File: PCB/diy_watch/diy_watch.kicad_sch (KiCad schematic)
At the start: 48 parts, among them IC1 W25Q16JVUXIQ, J1 USB_B_Micro, SW1 SW_Push, U1 FTE-2CA-V-T/R, U2 DS3231MZ, U3 RP2040, U7 XC6210B332MR, U8 LTC4071EMS8E_PBF, Y1 12MHz_crystal

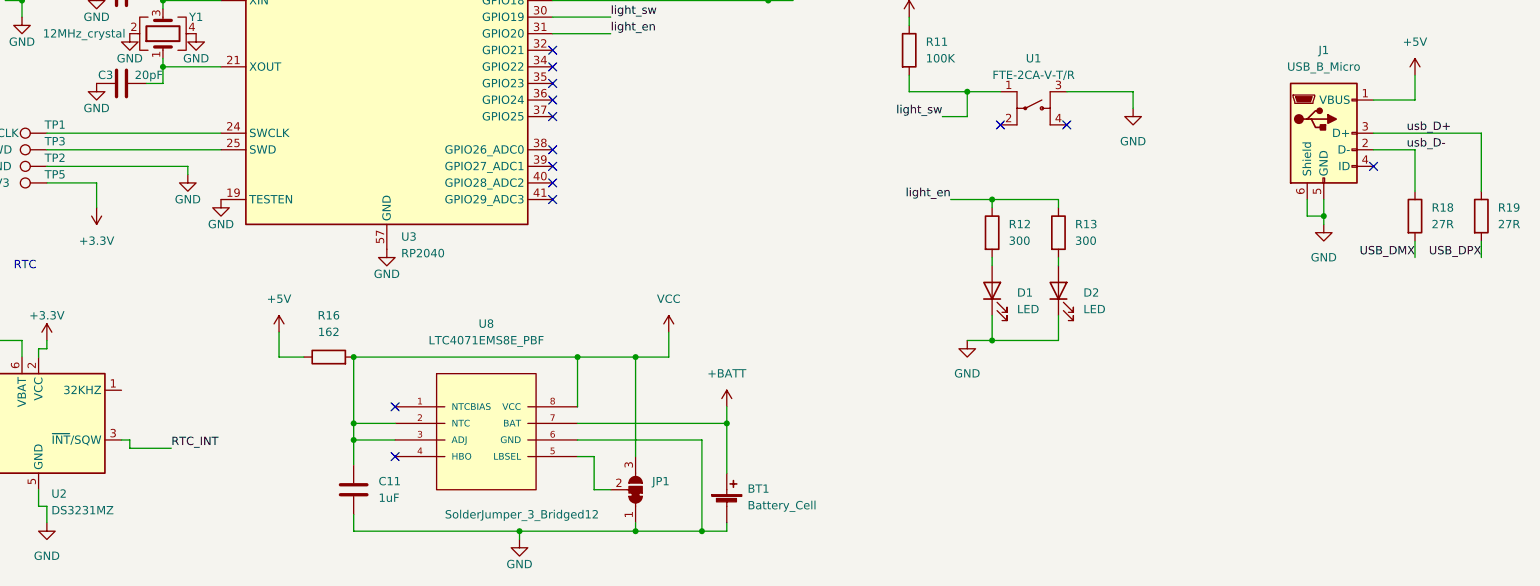
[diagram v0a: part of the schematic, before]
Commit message: Fixing DRC warnings
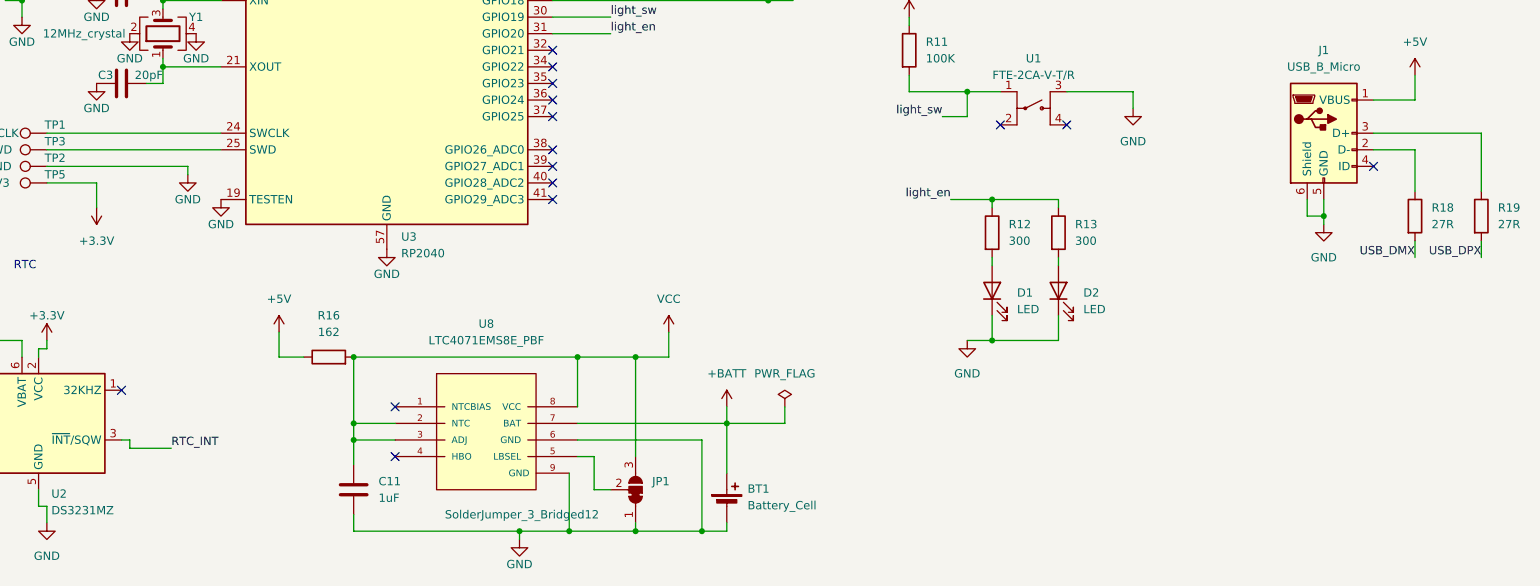
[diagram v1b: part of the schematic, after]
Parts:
- IC1: footprint DIY_Watch_lib:SON50P300X200X60-9N -> W25Q16JVUXIQ:SON50P300X200X60-9N
- U8: footprint Package_SO:MSOP-8-1EP_3x3mm_P0.65mm_EP1.5x1.8mm -> Package_SO:MSOP-8-1EP_3x3mm_P0.65mm_EP1.95x2.15mm
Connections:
- net GND: now also U8.9 (GND)
- net usb_D+: no longer names the net of J1.3 (D+), R19.1
- net usb_D-: no longer names the net of J1.2 (D-), R18.1
- no-connect marks 14 -> 15
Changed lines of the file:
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@@
 	)
 	(junction
+		(at 130.81 187.96)
+		(diameter 0)
+		(color 0 0 0 0)
+	)
+	(junction
 		(at 147.32 25.4)
 		(diameter 0)
@@
 	)
 	(no_connect
+		(at 62.23 166.37)
+	)
+	(no_connect
 		(at 128.27 121.92)
 	)
@@
 	(wire
 		(pts
+			(xy 163.83 171.45) (xy 154.94 171.45)
+		)
+		(stroke
+			(width 0)
+			(type default)
+		)
+	)
+	(wire
+		(pts
 			(xy 140.97 25.4) (xy 143.51 25.4)
 		)
@@
 	(wire
 		(pts
+			(xy 130.81 179.07) (xy 130.81 187.96)
+		)
+		(stroke
+			(width 0)
+			(type default)
+		)
+	)
+	(wire
+		(pts
 			(xy 200.66 78.74) (xy 208.28 78.74)
 		)
@@
 	(wire
 		(pts
-			(xy 123.19 187.96) (xy 140.97 187.96)
+			(xy 123.19 187.96) (xy 130.81 187.96)
 		)
 		(stroke
@@
 	(wire
 		(pts
+			(xy 130.81 187.96) (xy 140.97 187.96)
+		)
+		(stroke
+			(width 0)
+			(type default)
+		)
+	)
+	(wire
+		(pts
 			(xy 264.16 58.42) (xy 269.24 58.42)
 		)
@@
 	(wire
 		(pts
+			(xy 163.83 168.91) (xy 163.83 171.45)
+		)
+		(stroke
+			(width 0)
+			(type default)
+		)
+	)
+	(wire
+		(pts
 			(xy 128.27 66.04) (xy 137.16 66.04)
 		)
@@
 		)
 	)
-	(label "usb_D+"
-		(at 259.08 127 0)
-		(fields_autoplaced yes)
-		(effects
-			(font
-				(size 1.27 1.27)
-			)
-			(justify left bottom)
-		)
-		(property "Netclass" "usb"
-			(at 259.08 128.27 0)
-			(effects
-				(font
-					(size 1.27 1.27)
-					(italic yes)
-				)
-				(justify left)
-				(hide yes)
-			)
-		)
-	)
 	(label "USB_DMX"
 		(at 260.35 146.05 180)
-		(fields_autoplaced yes)
 		(effects
 			(font
@@
 			(justify right bottom)
 		)
-		(property "Netclass" "usb"
-			(at 260.35 147.32 0)
-			(effects
-				(font
-					(size 1.27 1.27)
-					(italic yes)
-				)
-				(justify right)
-				(hide yes)
-			)
-		)
 	)
 	(label "COM3"
@@
 		)
 	)
-	(label "usb_D-"
-		(at 259.08 129.54 0)
-		(fields_autoplaced yes)
-		(effects
-			(font
-				(size 1.27 1.27)
-			)
-			(justify left bottom)
-		)
-		(property "Netclass" "usb"
-			(at 259.08 130.81 0)
-			(effects
-				(font
-					(size 1.27 1.27)
-					(italic yes)
-				)
-				(justify left)
-				(hide yes)
-			)
-		)
-	)
 	(label "RTC_SCL"
 		(at 31.75 167.64 180)
@@
 	(label "USB_DPX"
 		(at 270.51 146.05 180)
-		(fields_autoplaced yes)
 		(effects
 			(font
@@
 			(justify right bottom)
 		)
-		(property "Netclass" "usb"
-			(at 270.51 147.32 0)
-			(effects
-				(font
-					(size 1.27 1.27)
-					(italic yes)
-				)
-				(justify right)
-				(hide yes)
-			)
-		)
 	)
 	(label "J"
@@
 	(label "USB_DMX"
 		(at 77.47 71.12 180)
-		(fields_autoplaced yes)
 		(effects
 			(font
@@
 			(justify right bottom)
 		)
-		(property "Netclass" "usb"
-			(at 77.47 72.39 0)
-			(effects
-				(font
-					(size 1.27 1.27)
-					(italic yes)
-				)
-				(justify right)
-				(hide yes)
-			)
-		)
 	)
 	(label "A"
@@
 	(label "USB_DPX"
 		(at 77.47 68.58 180)
-		(fields_autoplaced yes)
 		(effects
 			(font
@@
 			(justify right bottom)
 		)
-		(property "Netclass" "usb"
-			(at 77.47 69.85 0)
-			(effects
-				(font
-					(size 1.27 1.27)
-					(italic yes)
-				)
-				(justify right)
-				(hide yes)
-			)
-		)
 	)
 	(label "COM1"
@@
 			)
 		)
-		(property "Footprint" "DIY_Watch_lib:SON50P300X200X60-9N"
+		(property "Footprint" "W25Q16JVUXIQ:SON50P300X200X60-9N"
 			(at 40.64 45.72 0)
 			(effects
@@
 			)
 		)
-		(property "Footprint" "Package_SO:MSOP-8-1EP_3x3mm_P0.65mm_EP1.5x1.8mm"
+		(property "Footprint" "Package_SO:MSOP-8-1EP_3x3mm_P0.65mm_EP1.95x2.15mm"
 			(at 76.2 146.05 0)
 			(effects
@@
 		(pin "8"
 		)
+		(pin "9"
+		)
 		(instances
 			(project "diy_watch"
@@
 			)
 		)
-		(property "Description" ""
+		(property "Description" "Power symbol creates a global label with name \"+BATT\""
 			(at 38.1 152.4 0)
 			(effects
@@
 			)
 		)
-		(property "Description" ""
+		(property "Description" "Single-cell battery"
 			(at 154.94 184.15 0)
 			(effects
@@
 	)
 	(symbol
+		(lib_id "power:PWR_FLAG")
+		(at 163.83 168.91 0)
+		(unit 1)
+		(exclude_from_sim no)
+		(in_bom yes)
+		(on_board yes)
+		(dnp no)
+		(fields_autoplaced yes)
+		(property "Reference" "#FLG01"
+			(at 163.83 167.005 0)
+			(effects
+				(font
+					(size 1.27 1.27)
+				)
+				(hide yes)
+			)
+		)
+		(property "Value" "PWR_FLAG"
+			(at 163.83 163.83 0)
+			(effects
+				(font
+					(size 1.27 1.27)
+				)
+			)
+		)
+		(property "Footprint" ""
+			(at 163.83 168.91 0)
+			(effects
+				(font
+					(size 1.27 1.27)
+				)
+				(hide yes)
+			)
+		)
+		(property "Datasheet" "~"
+			(at 163.83 168.91 0)
+			(effects
+				(font
+					(size 1.27 1.27)
+				)
+				(hide yes)
+			)
+		)
+		(property "Description" "Special symbol for telling ERC where power comes from"
+			(at 163.83 168.91 0)
+			(effects
+				(font
+					(size 1.27 1.27)
+				)
+				(hide yes)
+			)
+		)
+		(pin "1"
+		)
+		(instances
+			(project ""
+				(path "/12c7509a-2a16-4dc7-8785-00872e5a9f11"
+					(reference "#FLG01")
+					(unit 1)
+				)
+			)
+		)
+	)
+	(symbol
 		(lib_id "MCU_RaspberryPi:RP2040")
 		(at 102.87 99.06 0)
@@
 			)
 		)
-		(property "Description" ""
+		(property "Description" "Power symbol creates a global label with name \"+BATT\""
 			(at 154.94 168.91 0)
 			(effects

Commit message: More DRC fixes
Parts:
- JP1: footprint Jumper:SolderJumper-3_P1.3mm_Bridged12_Pad1.0x1.5mm -> Jumper:SolderJumper-3_P1.3mm_Bridged12_RoundedPad1.0x1.5mm
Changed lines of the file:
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@@
 			)
 		)
-		(property "Footprint" "Jumper:SolderJumper-3_P1.3mm_Bridged12_Pad1.0x1.5mm"
+		(property "Footprint" "Jumper:SolderJumper-3_P1.3mm_Bridged12_RoundedPad1.0x1.5mm"
 			(at 140.97 181.61 0)
 			(effects

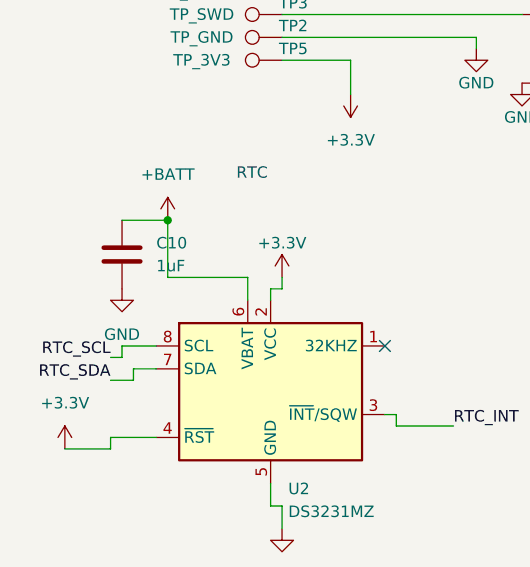
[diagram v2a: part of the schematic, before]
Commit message: Adding JLC part numbers to schematic
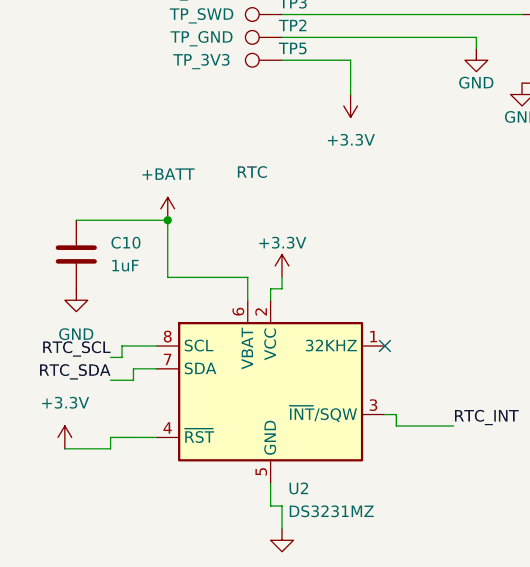
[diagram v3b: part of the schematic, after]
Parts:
- D1, D2: JLCPCB Part (none) -> C2296
- R1: JLCPCB Part (none) -> C11702
- R10, R3, R4, R5, R6, R7, R8, R9: JLCPCB Part (none) -> C25900
- R12, R13: JLCPCB Part (none) -> C25104
- R15, R17, R2: JLCPCB Part (none) -> C25744
- R16: JLCPCB Part (none) -> C25091
- R18, R19: JLCPCB Part (none) -> C25100
- U2: JLCPCB Part (none) -> C107410
- U3: JLCPCB Part (none) -> C2040
- U7: JLCPCB Part (none) -> C47719
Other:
- moved on the sheet: C10
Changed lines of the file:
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@@
 	(wire
 		(pts
-			(xy 33.02 152.4) (xy 38.1 152.4)
+			(xy 27.94 152.4) (xy 38.1 152.4)
 		)
 		(stroke
@@
 	(symbol
 		(lib_id "power:GND")
-		(at 33.02 160.02 0)
+		(at 27.94 160.02 0)
 		(unit 1)
 		(exclude_from_sim no)
@@
 		(fields_autoplaced yes)
 		(property "Reference" "#PWR040"
-			(at 33.02 166.37 0)
+			(at 27.94 166.37 0)
 			(effects
 				(font
@@
 		)
 		(property "Value" "GND"
-			(at 33.02 165.1 0)
+			(at 27.94 165.1 0)
 			(effects
 				(font
@@
 		)
 		(property "Footprint" ""
-			(at 33.02 160.02 0)
+			(at 27.94 160.02 0)
 			(effects
 				(font
@@
 		)
 		(property "Datasheet" ""
-			(at 33.02 160.02 0)
+			(at 27.94 160.02 0)
 			(effects
 				(font
@@
 		)
 		(property "Description" "Power symbol creates a global label with name \"GND\" , ground"
-			(at 33.02 160.02 0)
+			(at 27.94 160.02 0)
 			(effects
 				(font
@@
 			)
 		)
+		(property "JLCPCB Part" "C25900"
+			(at 208.28 52.07 0)
+			(effects
+				(font
+					(size 1.27 1.27)
+				)
+				(hide yes)
+			)
+		)
 		(pin "1"
 		)
@@
 			)
 		)
+		(property "JLCPCB Part" "C25104"
+			(at 195.58 142.24 0)
+			(effects
+				(font
+					(size 1.27 1.27)
+				)
+				(hide yes)
+			)
+		)
 		(pin "1"
 		)
@@
 			)
 		)
+		(property "JLCPCB Part" "C25091"
+			(at 93.98 161.29 90)
+			(effects
+				(font
+					(size 1.27 1.27)
+				)
+				(hide yes)
+			)
+		)
 		(pin "1"
 		)
@@
 			)
 		)
+		(property "JLCPCB Part" "C25900"
+			(at 215.9 52.07 0)
+			(effects
+				(font
+					(size 1.27 1.27)
+				)
+				(hide yes)
+			)
+		)
 		(pin "1"
 		)
@@
 			)
 		)
+		(property "JLCPCB Part" "C25900"
+			(at 200.66 72.39 0)
+			(effects
+				(font
+					(size 1.27 1.27)
+				)
+				(hide yes)
+			)
+		)
 		(pin "1"
 		)
@@
 			)
 		)
+		(property "JLCPCB Part" "C47719"
+			(at 162.56 27.94 0)
+			(effects
+				(font
+					(size 1.27 1.27)
+				)
+				(hide yes)
+			)
+		)
 		(pin "1"
 		)
@@
 	(symbol
 		(lib_id "Device:C")
-		(at 33.02 156.21 0)
+		(at 27.94 156.21 0)
 		(unit 1)
 		(exclude_from_sim no)
@@
 		(fields_autoplaced yes)
 		(property "Reference" "C10"
-			(at 36.83 154.94 0)
+			(at 31.75 154.94 0)
 			(effects
 				(font
@@
 		)
 		(property "Value" "1uF"
-			(at 36.83 157.48 0)
+			(at 31.75 157.48 0)
 			(effects
 				(font
@@
 		)
 		(property "Footprint" "Capacitor_SMD:C_0402_1005Metric"
-			(at 33.9852 160.02 0)
+			(at 28.9052 160.02 0)
 			(effects
 				(font
@@
 		)
 		(property "Datasheet" "~"
-			(at 33.02 156.21 0)
+			(at 27.94 156.21 0)
 			(effects
 				(font
@@
 		)
 		(property "Description" ""
-			(at 33.02 156.21 0)
+			(at 27.94 156.21 0)
 			(effects
 				(font
@@
 		)
 		(property "JLCPCB Part" "C52923 "
-			(at 33.02 156.21 0)
+			(at 27.94 156.21 0)
 			(effects
 				(font
@@
 			)
 		)
+		(property "JLCPCB Part" "C25900"
+			(at 215.9 72.39 0)
+			(effects
+				(font
+					(size 1.27 1.27)
+				)
+				(hide yes)
+			)
+		)
 		(pin "1"
 		)
@@
 			)
 		)
+		(property "JLCPCB Part" "C25100"
+			(at 270.51 139.7 0)
+			(effects
+				(font
+					(size 1.27 1.27)
+				)
+				(hide yes)
+			)
+		)
 		(pin "1"
 		)
@@
 			)
 		)
+		(property "JLCPCB Part" "C25900"
+			(at 208.28 72.39 0)
+			(effects
+				(font
+					(size 1.27 1.27)
+				)
+				(hide yes)
+			)
+		)
 		(pin "1"
 		)
@@
 			)
 		)
+		(property "JLCPCB Part" "C25100"
+			(at 260.35 139.7 0)
+			(effects
+				(font
+					(size 1.27 1.27)
+				)
+				(hide yes)
+			)
+		)
 		(pin "1"
 		)
@@
 			)
 		)
+		(property "JLCPCB Part" "C25900"
+			(at 223.52 52.07 0)
+			(effects
+				(font
+					(size 1.27 1.27)
+				)
+				(hide yes)
+			)
+		)
 		(pin "1"
 		)
@@
 			)
 		)
+		(property "JLCPCB Part" "C25900"
+			(at 200.66 52.07 0)
+			(effects
+				(font
+					(size 1.27 1.27)
+				)
+				(hide yes)
+			)
+		)
 		(pin "1"
 		)
@@
 			)
 		)
+		(property "JLCPCB Part" "C2040 "
+			(at 102.87 99.06 0)
+			(effects
+				(font
+					(size 1.27 1.27)
+				)
+				(hide yes)
+			)
+		)
 		(pin "1"
 		)
@@
 			)
 		)
+		(property "JLCPCB Part" "C25900"
+			(at 223.52 72.39 0)
+			(effects
+				(font
+					(size 1.27 1.27)
+				)
+				(hide yes)
+			)
+		)
 		(pin "1"
 		)
@@
 			)
 		)
+		(property "JLCPCB Part" "C25744"
+			(at 143.51 95.25 0)
+			(effects
+				(font
+					(size 1.27 1.27)
+				)
+				(hide yes)
+			)
+		)
 		(pin "1"
 		)
@@
 			)
 		)
+		(property "JLCPCB Part" "C2296"
+			(at 205.74 151.13 90)
+			(effects
+				(font
+					(size 1.27 1.27)
+				)
+				(hide yes)
+			)
+		)
 		(pin "1"
 		)
@@
 			)
 		)
+		(property "JLCPCB Part" "C2296"
+			(at 195.58 151.13 90)
+			(effects
+				(font
+					(size 1.27 1.27)
+				)
+				(hide yes)
+			)
+		)
 		(pin "1"
 		)
@@
 			)
 		)
+		(property "JLCPCB Part" "C25744"
+			(at 152.4 95.25 0)
+			(effects
+				(font
+					(size 1.27 1.27)
+				)
+				(hide yes)
+			)
+		)
 		(pin "1"
 		)
@@
 			)
 		)
+		(property "JLCPCB Part" "C25104"
+			(at 205.74 142.24 0)
+			(effects
+				(font
+					(size 1.27 1.27)
+				)
+				(hide yes)
+			)
+		)
 		(pin "1"
 		)
@@
 			)
 		)
+		(property "JLCPCB Part" "C107410"
+			(at 49.53 171.45 0)
+			(effects
+				(font
+					(size 1.27 1.27)
+				)
+				(hide yes)
+			)
+		)
 		(pin "1"
 		)
@@
 			)
 		)
+		(property "JLCPCB Part" "C25744"
+			(at 161.29 95.25 0)
+			(effects
+				(font
+					(size 1.27 1.27)
+				)
+				(hide yes)
+			)
+		)
 		(pin "1"
 		)
@@
 			(at 59.69 68.58 0)
 			(effects
+				(font
+					(size 1.27 1.27)
+				)
+				(hide yes)
+			)
+		)
+		(property "JLCPCB Part" "C11702 "
+			(at 59.69 68.58 0)
+			(effects
